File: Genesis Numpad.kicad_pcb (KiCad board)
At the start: 2 copper layers, 107.2 x 123 mm, 56 parts, among them SW1 SW_Push, U1 ATmega32U4-AU, Y1 16MHz

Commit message: Unfricked some power lines
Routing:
- net +5V: track 96.9 -> 124.3 mm, vias 2 -> 7
- net GND: track 50.6 -> 45.5 mm, vias 4 -> 0
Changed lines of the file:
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@@
     (thickness 1.6)
     (drawings 17)
-    (tracks 476)
+    (tracks 482)
     (zones 0)
     (modules 56)
@@
   (segment (start 124.233332 24.537166) (end 124.550249 24.220249) (width 0.381) (layer B.Cu) (net 1))
   (segment (start 124.233332 27.272314) (end 124.233332 24.537166) (width 0.381) (layer B.Cu) (net 1))
-  (segment (start 119.566427 38.727444) (end 120.65 37.643871) (width 0.381) (layer B.Cu) (net 1))
-  (segment (start 129.3245 35.899017) (end 128.350483 34.925) (width 0.381) (layer B.Cu) (net 1))
   (segment (start 117.86937 31.232112) (end 118.418979 31.781721) (width 0.381) (layer B.Cu) (net 1))
-  (via (at 124.61875 35.71875) (size 0.8) (drill 0.4) (layers F.Cu B.Cu) (net 1))
   (segment (start 124.249408 36.088092) (end 124.61875 35.71875) (width 0.381) (layer B.Cu) (net 1))
-  (segment (start 124.249408 39.874891) (end 124.249408 36.088092) (width 0.381) (layer B.Cu) (net 1))
   (segment (start 124.799017 40.4245) (end 124.249408 39.874891) (width 0.381) (layer B.Cu) (net 1))
-  (segment (start 124.61875 35.71875) (end 124.61875 32.54375) (width 0.381) (layer F.Cu) (net 1))
-  (via (at 124.61875 32.54375) (size 0.8) (drill 0.4) (layers F.Cu B.Cu) (net 1))
-  (via (at 120.65 32.54375) (size 0.8) (drill 0.4) (layers F.Cu B.Cu) (net 1))
-  (segment (start 124.61875 32.54375) (end 120.65 32.54375) (width 0.381) (layer F.Cu) (net 1))
-  (via (at 120.904 37.211) (size 0.8) (drill 0.4) (layers F.Cu B.Cu) (net 1))
-  (segment (start 120.65 36.957) (end 120.904 37.211) (width 0.381) (layer F.Cu) (net 1))
-  (segment (start 120.65 32.54375) (end 120.65 36.957) (width 0.381) (layer F.Cu) (net 1))
   (segment (start 117.86937 31.232112) (end 117.846112 31.232112) (width 0.381) (layer B.Cu) (net 1))
   (segment (start 117.846112 31.232112) (end 116.967 30.353) (width 0.381) (layer B.Cu) (net 1))
@@
   (segment (start 134.14375 35.71875) (end 134.14375 34.925) (width 0.381) (layer B.Cu) (net 1))
   (segment (start 124.233332 27.272314) (end 124.233332 27.372918) (width 0.381) (layer B.Cu) (net 1))
-  (segment (start 124.233332 27.372918) (end 123.03125 28.575) (width 0.381) (layer B.Cu) (net 1))
+  (segment (start 129.3245 35.899017) (end 128.350483 34.925) (width 0.381) (layer B.Cu) (net 1))
+  (segment (start 124.249408 39.874891) (end 124.202891 39.874891) (width 0.381) (layer B.Cu) (net 1))
+  (segment (start 124.202891 39.874891) (end 123.444 39.116) (width 0.381) (layer B.Cu) (net 1))
+  (segment (start 119.566427 38.727444) (end 119.641556 38.727444) (width 0.381) (layer B.Cu) (net 1))
+  (segment (start 122.552353 38.177836) (end 124.799017 40.4245) (width 0.381) (layer B.Cu) (net 1))
+  (segment (start 120.191164 38.177836) (end 122.552353 38.177836) (width 0.381) (layer B.Cu) (net 1))
+  (segment (start 119.641556 38.727444) (end 120.191164 38.177836) (width 0.381) (layer B.Cu) (net 1))
+  (segment (start 125.4125 34.925) (end 124.249408 36.088092) (width 0.381) (layer B.Cu) (net 1))
+  (segment (start 128.350483 34.925) (end 125.4125 34.925) (width 0.381) (layer B.Cu) (net 1))
+  (segment (start 124.799017 40.4245) (end 124.799017 40.471017) (width 0.381) (layer B.Cu) (net 1))
+  (segment (start 124.799017 40.471017) (end 125.984 41.656) (width 0.381) (layer B.Cu) (net 1))
   (segment (start 125.893751 26.743266) (end 125.893751 25.563751) (width 0.381) (layer B.Cu) (net 2))
   (segment (start 124.799017 27.838) (end 125.893751 26.743266) (width 0.381) (layer B.Cu) (net 2))
@@
   (segment (start 130.080103 35.523249) (end 129.890186 35.333332) (width 0.381) (layer B.Cu) (net 2))
   (segment (start 132.424249 35.523249) (end 130.080103 35.523249) (width 0.381) (layer B.Cu) (net 2))
-  (segment (start 122.2375 30.399517) (end 124.799017 27.838) (width 0.381) (layer B.Cu) (net 2))
-  (segment (start 122.2375 33.793629) (end 122.2375 30.399517) (width 0.381) (layer B.Cu) (net 2))
-  (segment (start 128.350483 33.793629) (end 122.2375 33.793629) (width 0.381) (layer B.Cu) (net 2))
-  (segment (start 129.890186 35.333332) (end 128.350483 33.793629) (width 0.381) (layer B.Cu) (net 2))
-  (segment (start 121.813091 39.874892) (end 121.263483 40.4245) (width 0.381) (layer B.Cu) (net 2))
-  (segment (start 124.233332 40.990186) (end 123.118038 39.874892) (width 0.381) (layer B.Cu) (net 2))
-  (segment (start 122.843858 39.874892) (end 122.2375 39.268534) (width 0.381) (layer B.Cu) (net 2))
-  (segment (start 123.118038 39.874892) (end 122.843858 39.874892) (width 0.381) (layer B.Cu) (net 2))
-  (segment (start 122.843858 39.874892) (end 121.813091 39.874892) (width 0.381) (layer B.Cu) (net 2))
-  (segment (start 122.2375 35.71875) (end 121.27494 34.75619) (width 0.381) (layer B.Cu) (net 2))
-  (segment (start 122.2375 39.268534) (end 122.2375 35.71875) (width 0.381) (layer B.Cu) (net 2))
-  (segment (start 121.27494 34.75619) (end 122.2375 33.793629) (width 0.381) (layer B.Cu) (net 2))
-  (segment (start 119.417564 36.613564) (end 119.417564 36.359564) (width 0.381) (layer B.Cu) (net 2))
-  (segment (start 118.435056 37.596073) (end 119.417564 36.613564) (width 0.381) (layer B.Cu) (net 2))
-  (segment (start 119.417564 36.613564) (end 121.27494 34.75619) (width 0.381) (layer B.Cu) (net 2))
-  (segment (start 119.417564 36.359564) (end 117.983 34.925) (width 0.381) (layer B.Cu) (net 2))
-  (segment (start 117.983 32.477113) (end 117.303685 31.797798) (width 0.381) (layer B.Cu) (net 2))
-  (segment (start 117.983 34.925) (end 117.983 32.477113) (width 0.381) (layer B.Cu) (net 2))
+  (segment (start 122.588269 42.635249) (end 120.232249 42.635249) (width 0.381) (layer B.Cu) (net 2))
+  (segment (start 124.233332 40.990186) (end 122.588269 42.635249) (width 0.381) (layer B.Cu) (net 2))
+  (via (at 111.633 33.655) (size 0.8) (drill 0.4) (layers F.Cu B.Cu) (net 2))
+  (segment (start 114.935 36.957) (end 111.633 33.655) (width 0.381) (layer B.Cu) (net 2))
+  (segment (start 114.935 37.846) (end 114.935 36.957) (width 0.381) (layer B.Cu) (net 2))
+  (via (at 115.824 30.48) (size 0.8) (drill 0.4) (layers F.Cu B.Cu) (net 2))
+  (segment (start 114.808 30.48) (end 115.824 30.48) (width 0.381) (layer F.Cu) (net 2))
+  (segment (start 111.633 33.655) (end 114.808 30.48) (width 0.381) (layer F.Cu) (net 2))
+  (segment (start 115.985887 30.48) (end 117.303685 31.797798) (width 0.381) (layer B.Cu) (net 2))
+  (segment (start 115.824 30.48) (end 115.985887 30.48) (width 0.381) (layer B.Cu) (net 2))
+  (via (at 127.254 26.67) (size 0.8) (drill 0.4) (layers F.Cu B.Cu) (net 2))
+  (segment (start 116.078 37.846) (end 127.254 26.67) (width 0.381) (layer F.Cu) (net 2))
+  (segment (start 114.935 37.846) (end 116.078 37.846) (width 0.381) (layer F.Cu) (net 2))
+  (segment (start 127 26.67) (end 125.893751 25.563751) (width 0.381) (layer B.Cu) (net 2))
+  (segment (start 127.254 26.67) (end 127 26.67) (width 0.381) (layer B.Cu) (net 2))
+  (via (at 118.872 43.942) (size 0.8) (drill 0.4) (layers F.Cu B.Cu) (net 2))
+  (segment (start 114.935 40.005) (end 118.872 43.942) (width 0.381) (layer F.Cu) (net 2))
+  (segment (start 114.935 37.846) (end 114.935 40.005) (width 0.381) (layer F.Cu) (net 2))
+  (segment (start 118.925498 43.942) (end 120.232249 42.635249) (width 0.381) (layer B.Cu) (net 2))
+  (segment (start 118.872 43.942) (end 118.925498 43.942) (width 0.381) (layer B.Cu) (net 2))
+  (via (at 131.191 36.83) (size 0.8) (drill 0.4) (layers F.Cu B.Cu) (net 2))
+  (segment (start 124.079 43.942) (end 131.191 36.83) (width 0.381) (layer F.Cu) (net 2))
+  (segment (start 118.872 43.942) (end 124.079 43.942) (width 0.381) (layer F.Cu) (net 2))
+  (segment (start 131.191 36.756498) (end 132.424249 35.523249) (width 0.381) (layer B.Cu) (net 2))
+  (segment (start 131.191 36.83) (end 131.191 36.756498) (width 0.381) (layer B.Cu) (net 2))
   (segment (start 117.104002 25.8445) (end 117.0305 25.8445) (width 0.25) (layer B.Cu) (net 3))
   (segment (start 119.035751 23.912751) (end 117.104002 25.8445) (width 0.25) (layer B.Cu) (net 3))

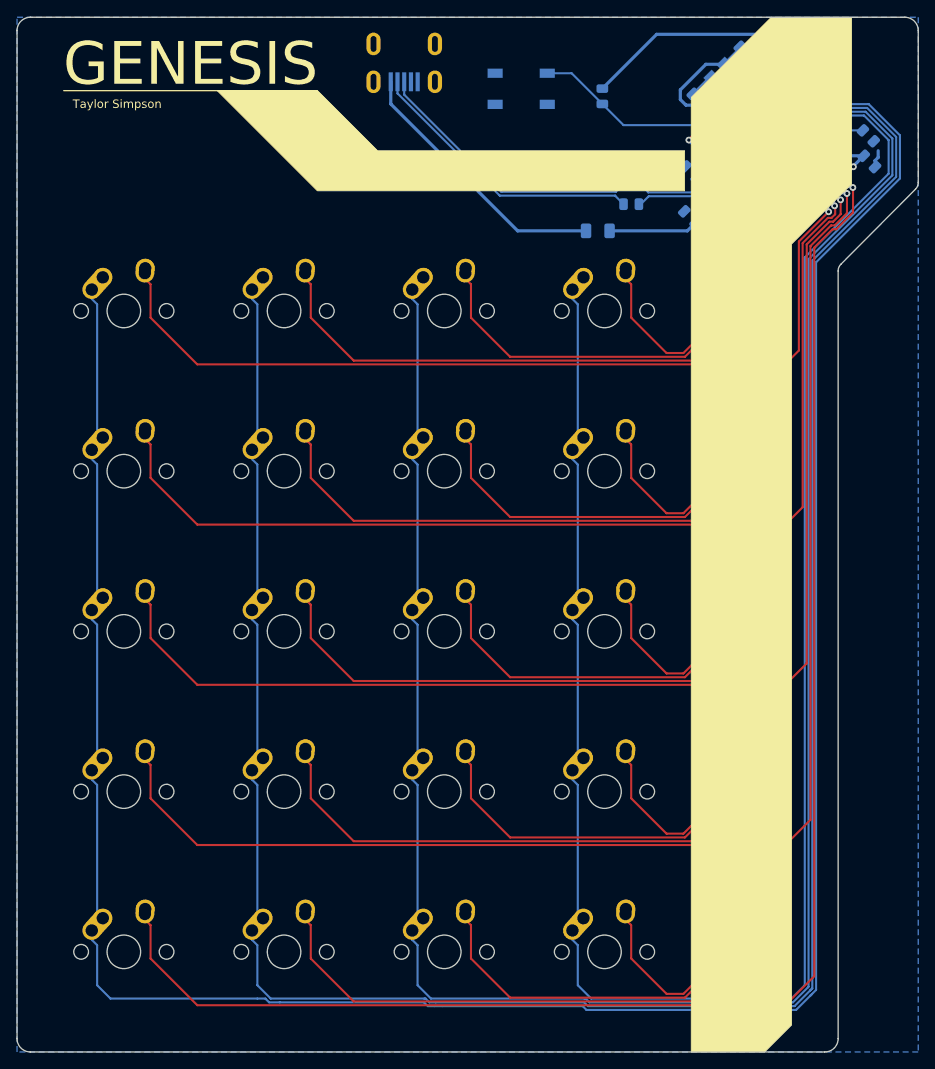
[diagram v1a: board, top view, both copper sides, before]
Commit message: Rerouted power
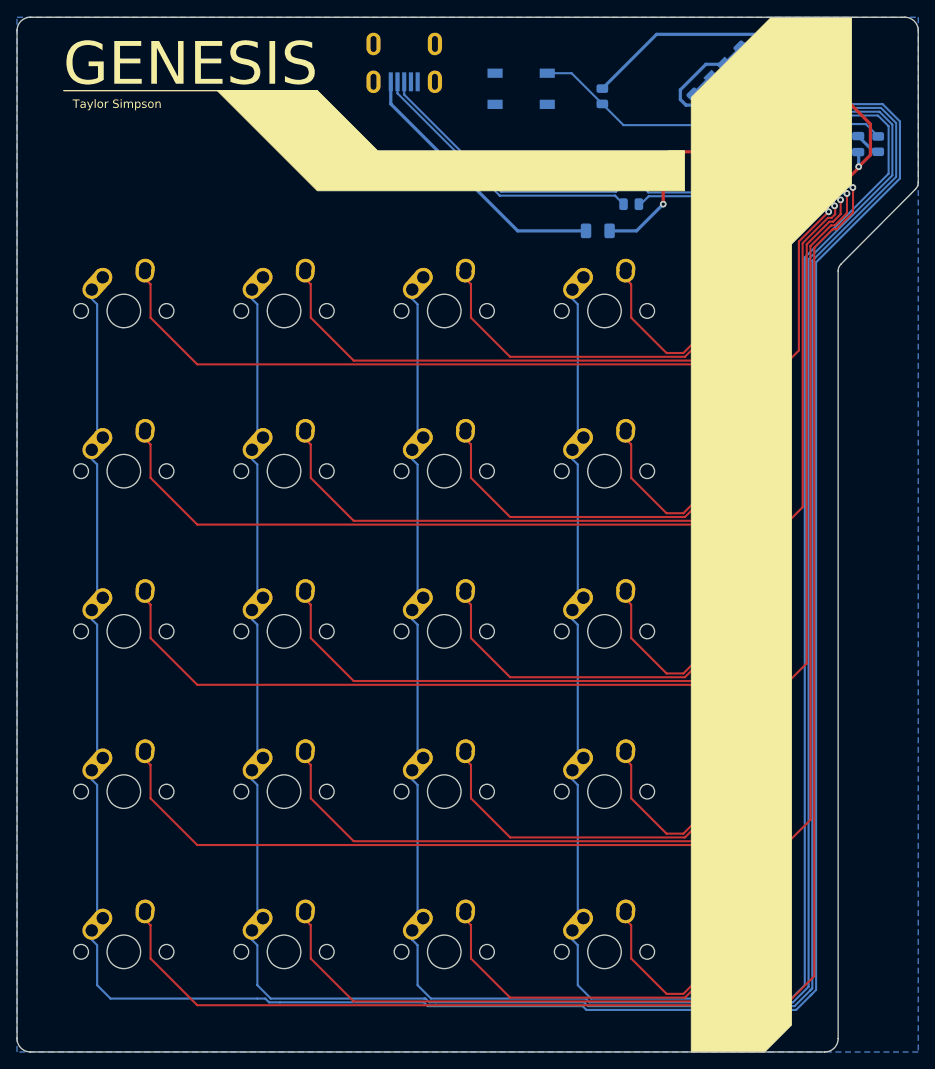
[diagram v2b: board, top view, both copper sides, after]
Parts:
- moved C6 9.03 mm to (114.3, 34.1), turned to 90 degrees
- moved C2 2.46 mm to (131.8, 34.1), turned to 90 degrees
- moved C1 2.25 mm to (123.0, 25.4), turned to 180 degrees
- moved C5 2.02 mm to (122.9, 42.9), turned to 180 degrees
- moved R4 1.53 mm to (134.1, 34.1), turned to 90 degrees
- moved C7 1.20 mm to (111.5, 38.6), turned to 180 degrees
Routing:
- net GND: track 45.5 -> 36.4 mm
- net Net-(R4-Pad2): track 2.61 -> 6.01 mm
- net COL0: track 284.2 -> 285.7 mm
- net COL1: track 262.9 -> 264.4 mm
- net COL2: track 241.4 -> 242.9 mm
- net +5V: track 124.3 -> 125.6 mm, vias 7 -> 6
- net COL3: track 220.2 -> 221.1 mm

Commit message: Fixed Bugs
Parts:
- moved C6 5.61 mm to (108.7, 34.9)
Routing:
- net +5V: vias 6 -> 7
